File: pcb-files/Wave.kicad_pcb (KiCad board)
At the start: 4 copper layers, 28 x 63.8 mm, 39 parts, among them IC1 NPM1300-QEAA-R, J1 USB4056-03-A_REVA2, J2 SJ-43516-SMT, J3 MEM2067-02-180-00-A_REVB, SW1 PTS815 SJM 250 SMTR LFS, SW2 PTS815 SJM 250 SMTR LFS, SW3 PTS815 SJM 250 SMTR LFS, U1 IM72D128V01XTMA1, U2 BT40F

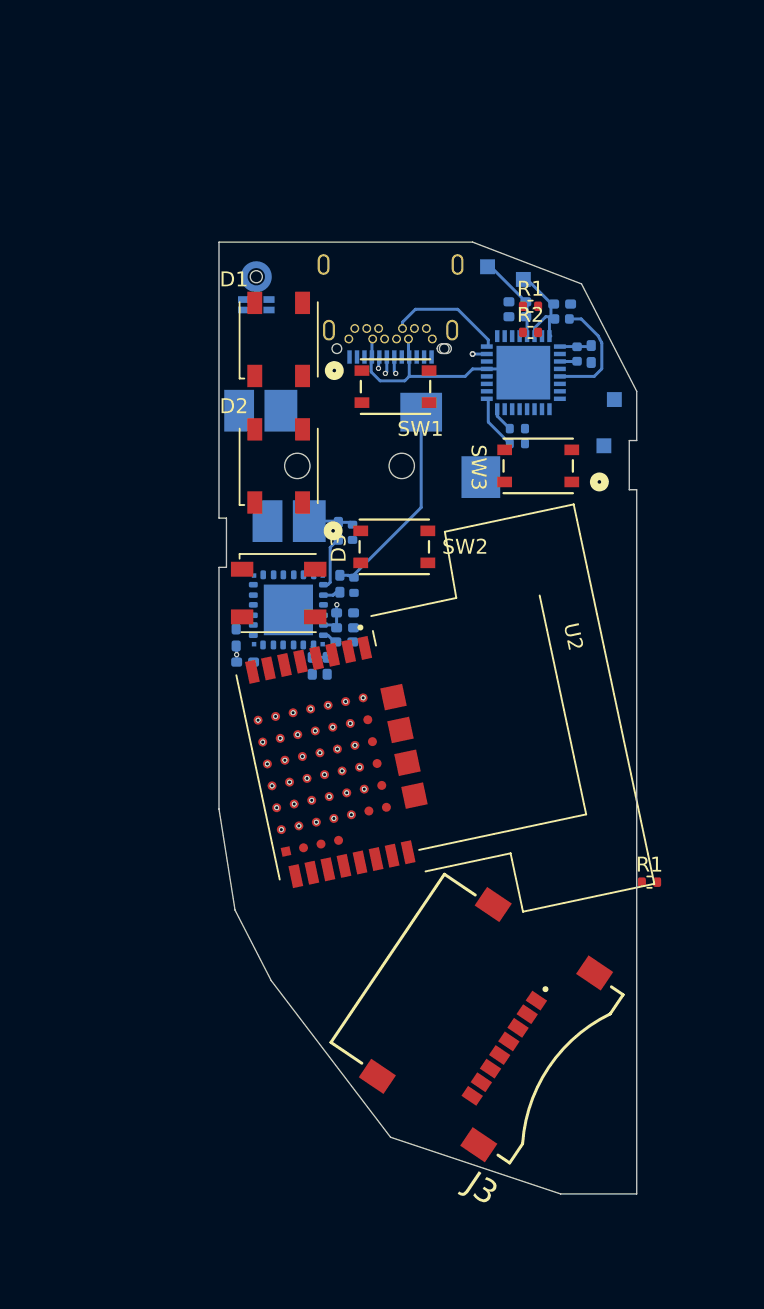
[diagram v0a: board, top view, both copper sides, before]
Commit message: Layout V1
First Layout of Wave v1
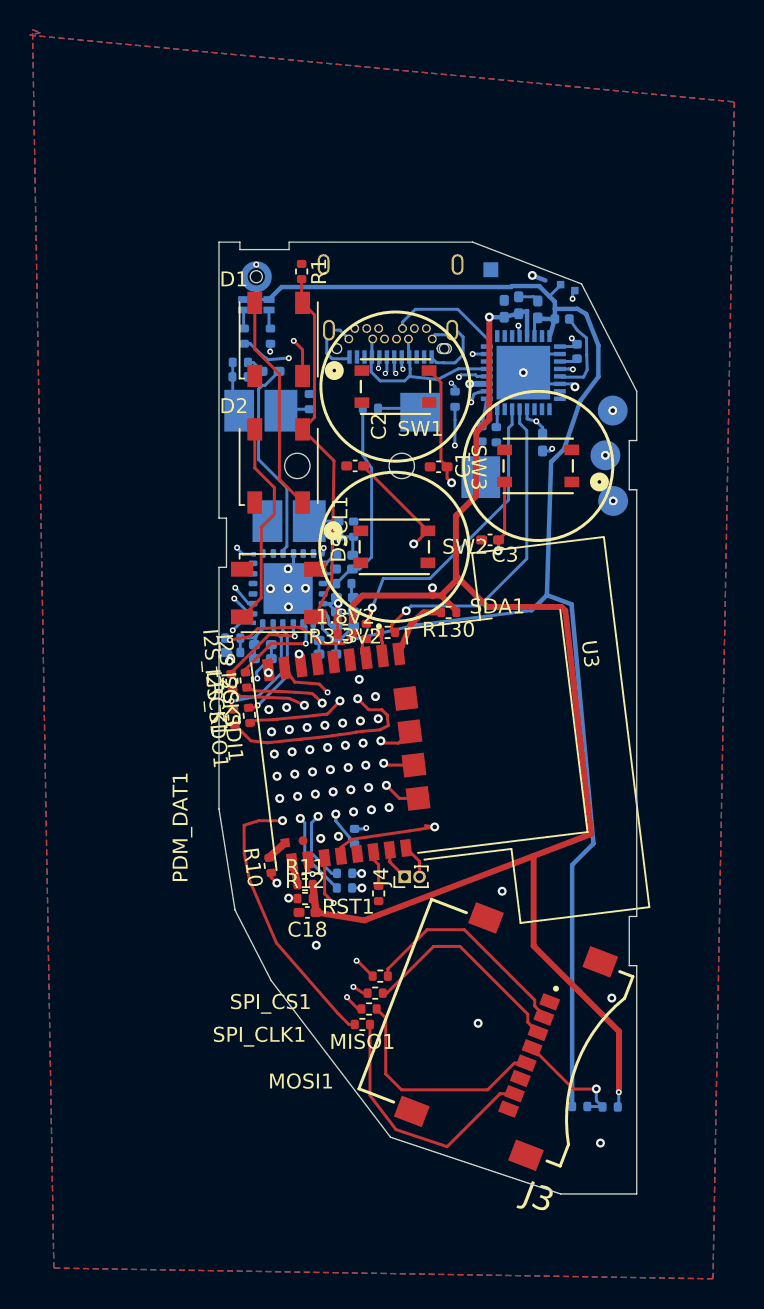
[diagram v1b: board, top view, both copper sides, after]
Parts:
- removed 3.3V1: TestPoint, TestPoint:TestPoint_Pad_1.0x1.0mm
- removed the R1 at (164.9, 112.9)
- removed the R1 at (145.1, 93.0)
- removed the U3 at (140.7, 94.7)
- added 1.8V2: 0, Resistor_SMD:R_0402_1005Metric, F.Cu at (144.5, 96.3)
- added 1.8V3: 1.8V, TestPoint:TestPoint_Pad_1.0x1.0mm, B.Cu at (158.9, 72.8)
- added 1.8V4: 0, Resistor_SMD:R_0402_1005Metric, B.Cu at (136.9, 96.5)
- added C12: 10uF, Capacitor_SMD:C_0402_1005Metric_Pad0.74x0.62mm_HandSolder, B.Cu at (155.1, 74.5)
- added C13: 10uF, Capacitor_SMD:C_0402_1005Metric_Pad0.74x0.62mm_HandSolder, B.Cu at (156.1, 74.2)
- added C14: 0.1uf, Capacitor_SMD:C_0402_1005Metric_Pad0.74x0.62mm_HandSolder, B.Cu at (143.3, 97.6)
- added C15: 0.1uf, Capacitor_SMD:C_0402_1005Metric_Pad0.74x0.62mm_HandSolder, B.Cu at (138.9, 97.9)
- added C16: 10uF, Capacitor_SMD:C_0402_1005Metric_Pad0.74x0.62mm_HandSolder, B.Cu at (143.3, 96.7)
- added C17: 10uF, Capacitor_SMD:C_0402_1005Metric_Pad0.74x0.62mm_HandSolder, B.Cu at (138.9, 97.0)
- added C18: .1uF, Capacitor_SMD:C_0402_1005Metric_Pad0.74x0.62mm_HandSolder, F.Cu at (141.9, 114.9)
- added D+1: 0, Resistor_SMD:R_0402_1005Metric, B.Cu at (144.4, 112.3)
- added D-1: 0, Resistor_SMD:R_0402_1005Metric, B.Cu at (144.4, 113.3)
- added I2S_LRCK1: 0, Resistor_SMD:R_0402_1005Metric, F.Cu at (136.9, 99.4)
- added I2S_SCK1: 0, Resistor_SMD:R_0402_1005Metric, F.Cu at (137.8, 99.3)
- added I2S_SDI1: 0, Resistor_SMD:R_0402_1005Metric, F.Cu at (138.0, 101.7)
- added I2S_SDO1: 0, Resistor_SMD:R_0402_1005Metric, F.Cu at (137.0, 101.8)
- added J4: Conn_01x02, Connector_PinHeader_1.00mm:PinHeader_1x02_P1.00mm_Vertical, F.Cu at (148.4, 112.5)
- added MIC_CLK1: 0, Resistor_SMD:R_0402_1005Metric, B.Cu at (137.7, 76.3)
- added MIC_DAT1: 0, Resistor_SMD:R_0402_1005Metric, B.Cu at (139.4, 76.3)
- added MISO1: 0, Resistor_SMD:R_0402_1005Metric, F.Cu at (145.6, 122.4)
- added MOSI1: 0, Resistor_SMD:R_0402_1005Metric, F.Cu at (146.5, 120.3)
- added PAD1: NTC, TestPoint:TestPoint_Pad_D2.0mm, B.Cu at (162.4, 87.3)
- added PAD2: VBAT, TestPoint:TestPoint_Pad_D2.0mm, B.Cu at (161.9, 84.3)
- added PAD3: GND, TestPoint:TestPoint_Pad_D2.0mm, B.Cu at (162.4, 81.3)
- added PAD4: GND, Battery:Battery_CR1225, B.Cu at (163.9, 127.3)
- added PDM_CLK1: 0, Resistor_SMD:R_0402_1005Metric, B.Cu at (151.8, 80.5)
- added PDM_DAT1: 0, Resistor_SMD:R_0402_1005Metric, B.Cu at (145.1, 109.8)
- added R10: 0, Resistor_SMD:R_0402_1005Metric, F.Cu at (139.4, 111.8)
- added R11: 0, Resistor_SMD:R_0402_1005Metric, F.Cu at (141.8, 113.1)
- added R12: 0, Resistor_SMD:R_0402_1005Metric, F.Cu at (141.8, 114.0)
- added R130: 0, Resistor_SMD:R_0402_1005Metric, F.Cu at (151.4, 94.8)
- added R3.3V1: 0, Resistor_SMD:R_0402_1005Metric, B.Cu at (162.2, 128.0)
- added R3.3V2: 0, Resistor_SMD:R_0402_1005Metric, F.Cu at (144.5, 95.3)
- added R3.3V3: 0, Resistor_SMD:R_0402_1005Metric, B.Cu at (136.9, 97.5)
- added R7: R, Resistor_SMD:R_0402_1005Metric, B.Cu at (144.4, 92.9)
- added R8: 4.7k, Resistor_SMD:R_0402_1005Metric, B.Cu at (154.6, 82.9)
- added R9: 10k, Resistor_SMD:R_0402_1005Metric, B.Cu at (153.6, 82.8)
- added RST1: 0, Resistor_SMD:R_0402_1005Metric, F.Cu at (146.7, 113.7)
- added SCL1: 0, Resistor_SMD:R_0402_1005Metric, F.Cu at (145.9, 96.1)
- added SDA1: 0, Resistor_SMD:R_0402_1005Metric, F.Cu at (147.3, 96.2)
- added SPI_CLK1: 0, Resistor_SMD:R_0402_1005Metric, F.Cu at (146.1, 121.4)
- added SPI_CS1: 0, Resistor_SMD:R_0402_1005Metric, F.Cu at (146.8, 119.2)
- added U2: ~, WAVE:WAVE_CODEC, B.Cu at (140.6, 93.2)
- 1.8V1: value 1.8V -> 0; footprint TestPoint:TestPoint_Pad_1.0x1.0mm -> Resistor_SMD:R_0402_1005Metric
- C1, C2, C3: value 10uF -> 1uF; moved to F.Cu
- C10, C8: value 0.1uf -> 10uF
- C5: value 10uF -> 0.1uf
- IC1: footprint NPM1300:QFN50P500X500X90-33N -> WAVE:QFN50P500X500X90-33N
- R1, R2: value R -> 0
- R2: value R -> 0; moved to B.Cu
- R3: value 10k -> 0
- R4: value 4.7k -> 0
- R5: value 1k -> 0; footprint Capacitor_SMD:C_0402_1005Metric_Pad0.74x0.62mm_HandSolder -> Resistor_SMD:R_0402_1005Metric
- R6: value 1k -> R; footprint Capacitor_SMD:C_0402_1005Metric_Pad0.74x0.62mm_HandSolder -> Resistor_SMD:R_0402_1005Metric
- moved 1.8V1 55.6 mm to (160.2, 127.9)
- moved C7 25.8 mm to (157.4, 74.5), turned to -90 degrees
- moved C5 22.1 mm to (144.4, 93.8), turned to 180 degrees
- moved R2 19.7 mm to (137.4, 79.0)
- moved R5 19.0 mm to (146.2, 81.1)
- moved C6 17.2 mm to (139.5, 78.7)
- moved R1 15.5 mm to (141.5, 72.0), turned to -90 degrees
- moved R3 14.2 mm to (142.1, 80.7), turned to 90 degrees
- moved C3 14.2 mm to (154.2, 90.0), turned to 180 degrees
- moved GND1 14.0 mm to (154.2, 71.8)
- moved R4 13.7 mm to (144.0, 89.2), turned to -90 degrees
- moved R2 13.6 mm to (137.4, 78.1), turned to 0 degrees
- moved R6 10.7 mm to (145.0, 89.2)
- moved C4 9.37 mm to (157.7, 83.4), turned to 90 degrees
- moved C1 7.97 mm to (150.7, 85.1), turned to 180 degrees
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- renumbered U2 to U3
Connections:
- 1.8V1 pad 1: /1.8V -> Net-(J3-VDD)
- C1 pad 1: /TRRS_RNG1 -> /BUTT_UP
- C1 pad 2: Net-(U3-OUT1M) -> GND
- C10 pad 2: /1.8V -> Net-(U2-AVDD)
- C11 pad 2: /1.8V -> Net-(U2-VREF)
- C2 pad 1: /TRRS_TIP -> /BUTT_DOWN
- C2 pad 2: Net-(U3-OUT1P) -> GND
- C3 pad 1: GND -> /BUTT_RT
- C3 pad 2: /1.2V -> GND
- C4 pad 2: /1.8V -> /1.2V
- C5 pad 2: /3.3V -> Net-(U2-AVDD)
- C6 pad 1: GND -> /TRRS_SLV
- C6 pad 2: /3.3V -> /IN1P
- C7 pad 2: Net-(U3-VREF) -> /1.8V
- C8 pad 1: GND -> /TRRS_RNG1
- C8 pad 2: Net-(U3-DREG) -> /OUT1M
- C9 pad 1: GND -> /TRRS_TIP
- C9 pad 2: Net-(U3-DREG) -> /OUT1P
- IC1 pad 29: /VLDO -> /3.3V
- J1 pad A8: unconnected-(J1-SBU1-PadA8) -> /PDM_CLK_SBU
- J1 pad B8: unconnected-(J1-SBU2-PadB8) -> /PDM_DAT_SBU
- J2 pad 1: /TRRS_SLV -> Net-(J2-Pad1)
- J2 pad 2: /TRRS_TIP -> Net-(J2-Pad2)
- J2 pad 3: /TRRS_RNG1 -> Net-(J2-Pad3)
- J2 pad 4: GND -> Net-(J2-Pad4)
- J3 pad 2: unconnected-(J3-CD/DAT3-Pad2) -> /SPI_CS
- J3 pad 3: unconnected-(J3-CMD-Pad3) -> /SPI_MOSI
- J3 pad 4: unconnected-(J3-VDD-Pad4) -> Net-(J3-VDD)
- J3 pad 7: /SPI_MOSI -> /SPI_MISO
- R1 pad 1: /TRRS_TIP -> unconnected-(R1-Pad1)
- R1 pad 2: GND -> Net-(D1-VDD)
- R2 pad 1: GND -> Net-(J2-Pad1) (x2)
- R2 pad 2: /TRRS_RNG1 -> /TRRS_SLV (x2)
- R3 pad 1: Net-(IC1-VSET1) -> Net-(J2-Pad4)
- R4 pad 1: GND -> Net-(J2-Pad3)
- R4 pad 2: Net-(IC1-VSET2) -> /TRRS_RNG1
- R5 pad 1: Net-(U3-SCL) -> Net-(J2-Pad2)
- R5 pad 2: /1.8V -> /TRRS_TIP
- R6 pad 1: Net-(U3-SDA) -> GND
- R6 pad 2: /1.8V -> /TRRS_RNG1
- U1 pad 1: /PDM_DATA -> /PDM_DAT_MIC
- U1 pad 3: /PDM_CLK -> /PDM_CLK_MIC
- U3 pad 1: /SDA -> Net-(U3-P1.02)
- U3 pad 11: /SPI_MOSI -> Net-(U3-P0.09/MOSI)
- U3 pad 14: /RST -> Net-(U3-~{RESET})
- U3 pad 2: /SCL -> Net-(U3-P1.03)
- U3 pad 9: /3.3V -> Net-(U3-VDD)
- U3 pad A3: /SPI_SCLK -> Net-(U3-P0.08/SCK)
- U3 pad B3: unconnected-(U2-P0.14/IO1-PadB3) -> Net-(U3-P0.14/IO1)
- U3 pad B6: GND -> unconnected-(U3-P0.13/IO0-PadB6)
- U3 pad E0: /PDM_CLK_MIC -> Net-(U3-P1.04)
- U3 pad E1: /PDM_DAT_MIC -> Net-(U3-P1.05)
- U3 pad E2: /PDM_CLK_SBU -> Net-(U3-P1.06)
- U3 pad E3: /PDM_DAT_SBU -> Net-(U3-P1.07)
- U3 pad E4: /DP1 -> /DP2
- U3 pad E5: /DN1 -> /DN2
- U3 pad E6: /SPI_MISO -> Net-(U3-P0.10/MISO)
- U3 pad F3: /SPI_CS????? -> unconnected-(U3-P0.18/CSN-PadF3)
- U3 pad F4: /3.3V -> Net-(U3-VDDH)
- U3 pad F6: /VBUS_5V -> Net-(U3-VBUS)
- U3 pad Z1: /I2S_SDO -> Net-(U3-P1.10)
- U3 pad Z2: /I2S_SDI -> Net-(U3-P1.11)
- U3 pad Z3: /I2S_SCK -> Net-(U3-P1.12)
- U3 pad Z4: /I2S_LRCK -> Net-(U3-P1.13)
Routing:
- net /3.3V: track 3.14 -> 121.0 mm, vias 0 -> 5
- net /1.8V: track 19.2 -> 109.6 mm
- net /VBUSIN: track 14.2 -> 75.5 mm, vias 0 -> 1
- net /PDM_DAT_SBU: track 0.00 -> 52.4 mm
- net GND: track 0.00 -> 51.3 mm, vias 1 -> 25
- net Net-(U3-P1.04): track 0.00 -> 37.0 mm, vias 0 -> 2
- net /SDA: track 0.00 -> 35.6 mm, vias 0 -> 2
- net Net-(U3-P1.05): track 0.00 -> 35.5 mm, vias 0 -> 2
- net /BUTT_RT: track 0.00 -> 32.7 mm, vias 0 -> 2
- net /SCL: track 0.00 -> 31.4 mm, vias 0 -> 2
- net /BUTT_UP: track 0.00 -> 31.1 mm, vias 0 -> 2
- net Net-(U3-P1.06): track 0.00 -> 31.0 mm, vias 0 -> 2
- net /NeoPixels: track 0.00 -> 27.6 mm, vias 0 -> 2
- net Net-(U3-P0.08/SCK): track 0.00 -> 27.2 mm, vias 0 -> 2
- net Net-(D1-VDD): track 0.00 -> 24.4 mm
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- added copper zone on B.Cu, net GND
- added copper zone on F.Cu, net GND
- added copper zone on In1.Cu, net GND
- added copper zone on In2.Cu, net GND
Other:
- outline, holes or cut-outs redrawn

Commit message: Silkscreen update
Updated Silkscreen
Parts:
- renumbered PAD3 to GND, GND1 to GND, PAD1 to NTC, PAD2 to V
